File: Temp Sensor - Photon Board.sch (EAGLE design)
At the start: 6 parts

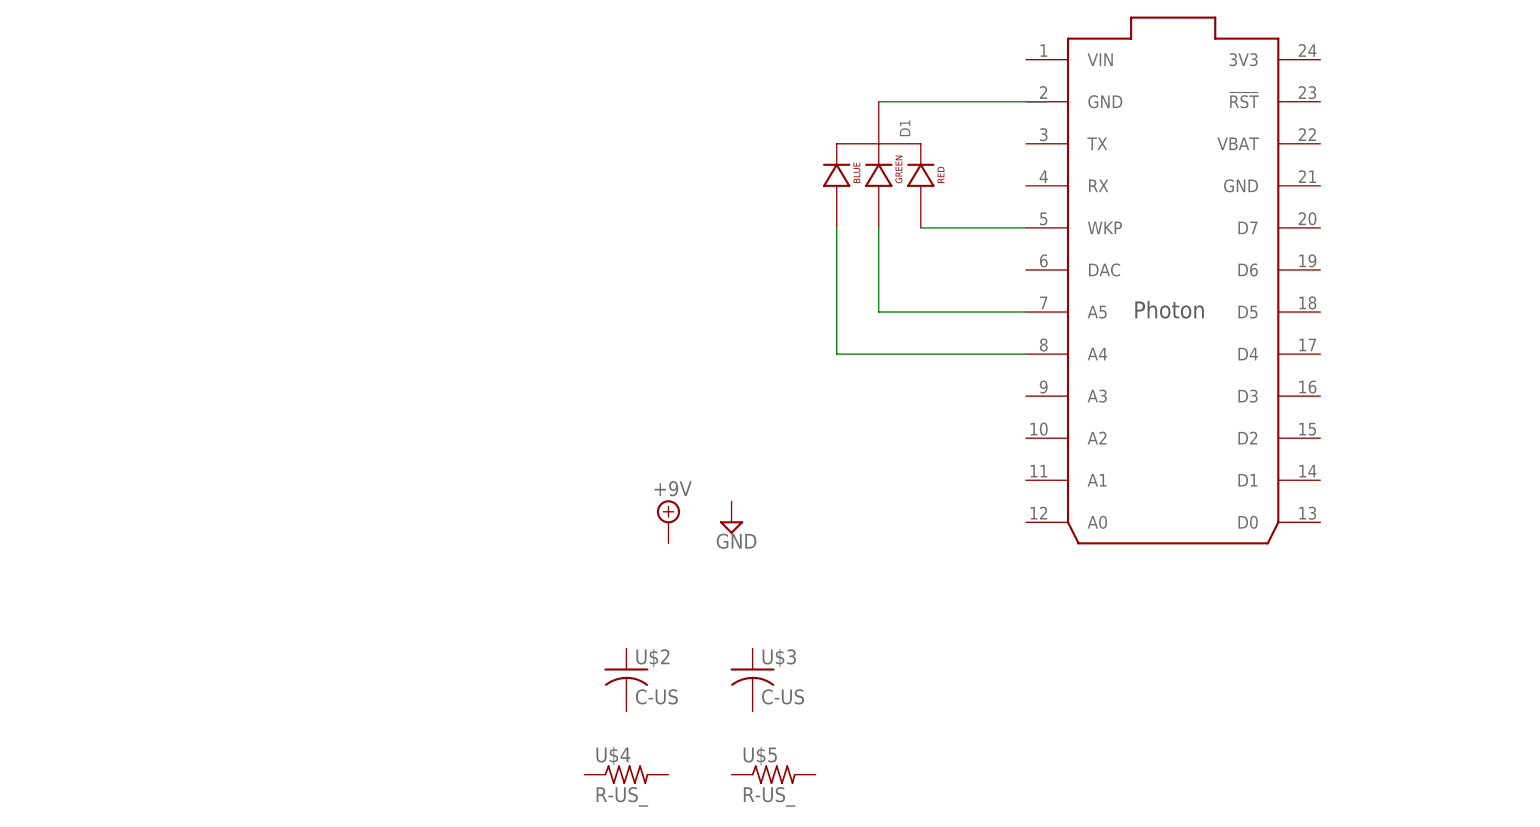
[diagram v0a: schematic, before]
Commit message: Added Photon Board schematics and board
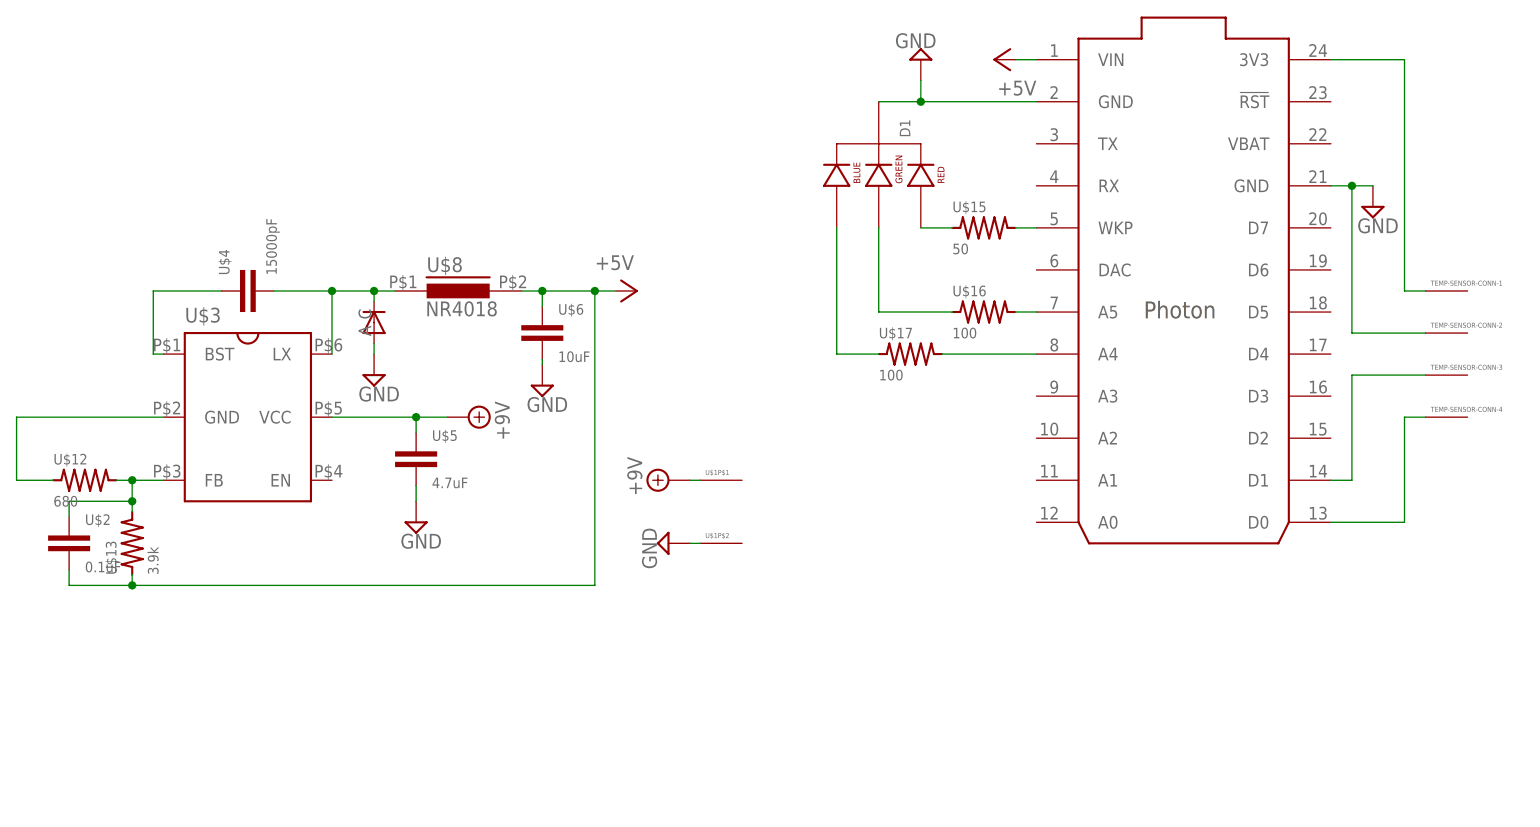
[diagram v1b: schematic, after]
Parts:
- added TEMP-SENSOR-CONN-: (no value), myhvac:S4B-PH-K-S
- added U$11: Photon w/ Headers, Spark:PHOTON_WITH_HEADERS
- added U$12: 680, myhvac:R0805
- added U$13: 3.9k, myhvac:R0805
- added U$15: 50, myhvac:R0805
- added U$16, U$17: 100, myhvac:R0805
- added U$6: 10uF, myhvac:FK16X7R1E106K
- added U$7: RK16, myhvac:RK16
- added U$8: NR4018, myhvac:NR4018
- D1: value LED-RGB-CC-THRUDIFFUSE -> LED-RGB-CC-THRU; device SparkFun-LED:LED-RGB-CC-THRUDIFFUSE -> myhvac:LED-RGB-CC-THRU
- U$1: value PHOTON_SMD -> (none); device Spark:PHOTON_SMD -> myhvac:S2B-PH-K-S
- U$2: value C-US -> 0.1uF; device Spark:C-US -> myhvac:K104Z15Y5VE5TL2
- U$3: value C-US -> (none); device Spark:C-US -> myhvac:BD9G101G-TR
- U$4: value R-US_ -> 15000pF; device Spark:R-US_ -> myhvac:K153K10X7RF5UH5
- U$5: value R-US_ -> 4.7uF; device Spark:R-US_ -> myhvac:FK28C0G1H4R7C
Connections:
- new net +5V: U$11.VIN, U$13.P$1, U$2.P$2, U$6.P$1, U$8.2
- new net +9V: U$1P$1.P$1, U$3.VCC, U$5.P$1
- new net GND: D1.CATHODE, TEMP-SENSOR-CONN-2.P$1, U$11.GND@2, U$11.GND@21, U$1P$2.P$1, U$5.P$2, U$6.P$2, U$7.ANODE
- new net N$11: U$11.A5, U$16.P$2
- new net N$12: U$11.A4, U$17.P$2
- new net N$13: D1.RED_CATHODE, U$15.P$1
- new net N$18: U$12.P$1, U$3.GND
- new net N$5: U$3.LX, U$4.P$2, U$7.CATHODE, U$8.1
- new net N$6: U$12.P$2, U$13.P$2, U$2.P$1, U$3.FB
- new net N$7: TEMP-SENSOR-CONN-1.P$1, U$11.3V3
- new net N$8: TEMP-SENSOR-CONN-3.P$1, U$11.D1
- new net N$9: TEMP-SENSOR-CONN-4.P$1, U$11.D0
- net N$1: now also U$11.WKP, U$15.P$2; no longer D1.RED_CATHODE, U$1G$1.WKP
- net N$2: now also U$16.P$1; no longer U$1G$1.A5
- net N$3: now also U$17.P$1; no longer U$1G$1.A4
- net N$4: now also U$3.BST, U$4.P$1; no longer D1.CATHODE

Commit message: Added Temp Sensor gerber files.  General cleanup or bck files
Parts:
- U$15: value 50 -> 100
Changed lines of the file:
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@@
 <part name="P+1" library="supply1" deviceset="+5V" device=""/>
 <part name="P+2" library="supply1" deviceset="+5V" device=""/>
-<part name="U$15" library="myhvac" deviceset="R0805" device="" value="50"/>
+<part name="U$15" library="myhvac" deviceset="R0805" device="" value="100"/>
 <part name="U$16" library="myhvac" deviceset="R0805" device="" value="100"/>
 <part name="U$17" library="myhvac" deviceset="R0805" device="" value="100"/>
@@
 </sheet>
 </sheets>
+<errors>
+</errors>
 </schematic>
 </drawing>

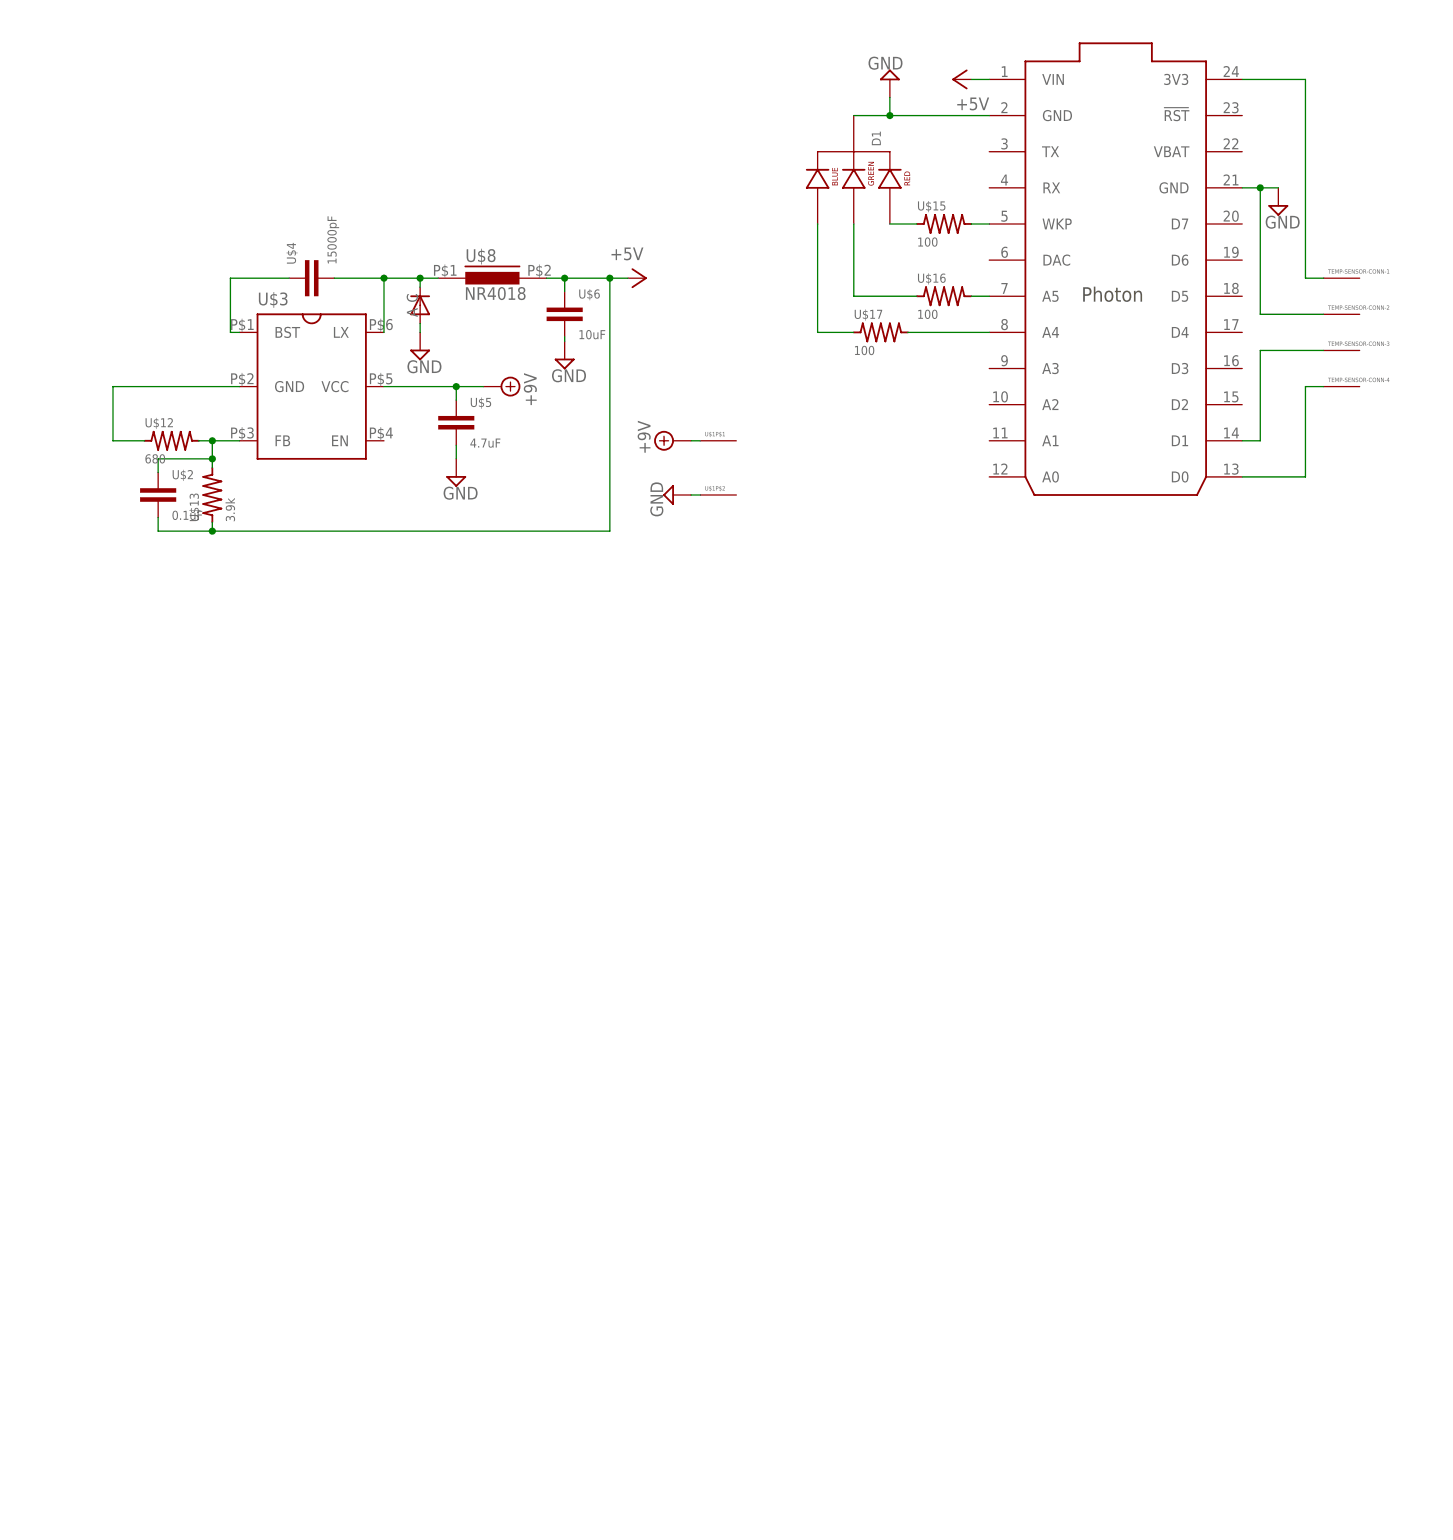
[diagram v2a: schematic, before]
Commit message: Modified the temp sensor to use a prebuilt power converter
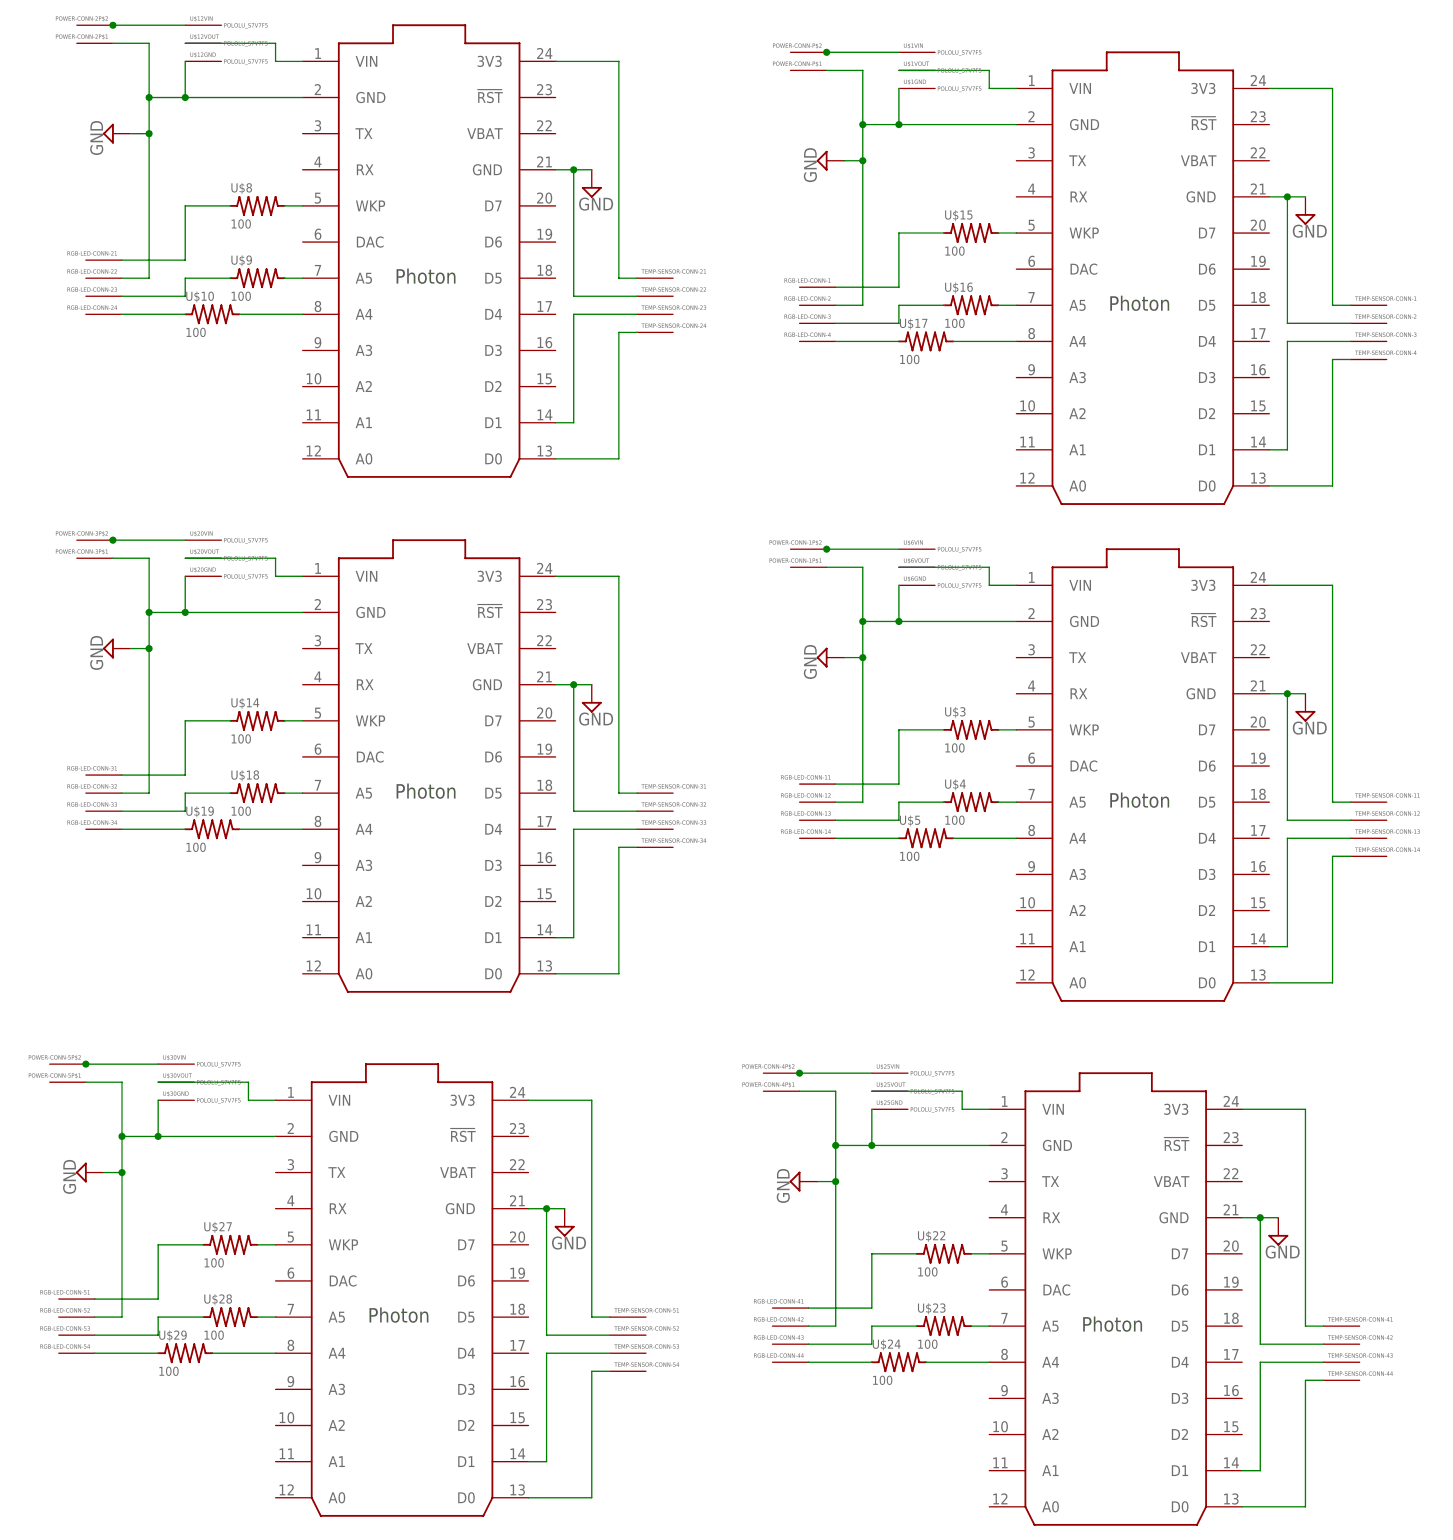
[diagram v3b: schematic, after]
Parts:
- removed D1: LED-RGB-CC-THRU, myhvac:LED-RGB-CC-THRU
- added POWER-CONN-, POWER-CONN-1, POWER-CONN-2, POWER-CONN-3, POWER-CONN-4, POWER-CONN-5: (no value), myhvac:S2B-PH-K-S
- added RGB-LED-CONN-, RGB-LED-CONN-1, RGB-LED-CONN-2, RGB-LED-CONN-3, RGB-LED-CONN-4, RGB-LED-CONN-5, TEMP-SENSOR-CONN-1, TEMP-SENSOR-CONN-2, TEMP-SENSOR-CONN-3, TEMP-SENSOR-CONN-4, TEMP-SENSOR-CONN-5: (no value), myhvac:S4B-PH-K-S
- added U$10, U$14, U$18, U$19, U$22, U$23, U$24, U$27, U$28, U$29, U$9: 100, myhvac:R0805
- added U$20, U$25, U$30: POLOLU_S7V7F5, myhvac:POLOLU_S7V7F5
- added U$21, U$26: Photon w/ Headers, Spark:PHOTON_WITH_HEADERS
- U$1: value (none) -> POLOLU_S7V7F5; device myhvac:S2B-PH-K-S -> myhvac:POLOLU_S7V7F5
- U$12: value 680 -> POLOLU_S7V7F5; device myhvac:R0805 -> myhvac:POLOLU_S7V7F5
- U$13: value 3.9k -> Photon w/ Headers; device myhvac:R0805 -> Spark:PHOTON_WITH_HEADERS
- U$2: value 0.1uF -> Photon w/ Headers; device myhvac:K104Z15Y5VE5TL2 -> Spark:PHOTON_WITH_HEADERS
- U$3: value (none) -> 100; device myhvac:BD9G101G-TR -> myhvac:R0805
- U$4: value 15000pF -> 100; device myhvac:K153K10X7RF5UH5 -> myhvac:R0805
- U$5: value 4.7uF -> 100; device myhvac:FK28C0G1H4R7C -> myhvac:R0805
- U$6: value 10uF -> POLOLU_S7V7F5; device myhvac:FK16X7R1E106K -> myhvac:POLOLU_S7V7F5
- U$7: value RK16 -> Photon w/ Headers; device myhvac:RK16 -> Spark:PHOTON_WITH_HEADERS
- U$8: value NR4018 -> 100; device myhvac:NR4018 -> myhvac:R0805
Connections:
- removed net +5V: U$11.VIN, U$13.P$1, U$2.P$2, U$6.P$1, U$8.2
- removed net +9V: U$1P$1.P$1, U$3.VCC, U$5.P$1
- new net N$10: RGB-LED-CONN-14.P$1, U$5.P$1
- new net N$14: TEMP-SENSOR-CONN-11.P$1, U$2.3V3
- new net N$15: TEMP-SENSOR-CONN-13.P$1, U$2.D1
- new net N$16: TEMP-SENSOR-CONN-14.P$1, U$2.D0
- new net N$17: U$2.WKP, U$3.P$2
- new net N$19: U$2.A4, U$5.P$2
- new net N$20: RGB-LED-CONN-11.P$1, U$3.P$1
- new net N$21: U$2.VIN, U$6VOUT.P$1
- new net N$22: POWER-CONN-1P$2.P$1, U$6VIN.P$1
- new net N$23: RGB-LED-CONN-23.P$1, U$9.P$1
- new net N$24: RGB-LED-CONN-24.P$1, U$10.P$1
- new net N$25: TEMP-SENSOR-CONN-21.P$1, U$7.3V3
- new net N$26: TEMP-SENSOR-CONN-23.P$1, U$7.D1
- new net N$27: TEMP-SENSOR-CONN-24.P$1, U$7.D0
- new net N$28: U$7.WKP, U$8.P$2
- new net N$29: U$7.A5, U$9.P$2
- new net N$30: U$10.P$2, U$7.A4
- new net N$31: RGB-LED-CONN-21.P$1, U$8.P$1
- new net N$32: U$12VOUT.P$1, U$7.VIN
- new net N$33: POWER-CONN-2P$2.P$1, U$12VIN.P$1
- new net N$34: RGB-LED-CONN-33.P$1, U$18.P$1
- new net N$35: RGB-LED-CONN-34.P$1, U$19.P$1
- new net N$36: TEMP-SENSOR-CONN-31.P$1, U$13.3V3
- new net N$37: TEMP-SENSOR-CONN-33.P$1, U$13.D1
- new net N$38: TEMP-SENSOR-CONN-34.P$1, U$13.D0
- new net N$39: U$13.WKP, U$14.P$2
- new net N$40: U$13.A5, U$18.P$2
- new net N$41: U$13.A4, U$19.P$2
- new net N$42: RGB-LED-CONN-31.P$1, U$14.P$1
- new net N$43: U$13.VIN, U$20VOUT.P$1
- new net N$44: POWER-CONN-3P$2.P$1, U$20VIN.P$1
- new net N$45: RGB-LED-CONN-43.P$1, U$23.P$1
- new net N$46: RGB-LED-CONN-44.P$1, U$24.P$1
- new net N$47: TEMP-SENSOR-CONN-41.P$1, U$21.3V3
- new net N$48: TEMP-SENSOR-CONN-43.P$1, U$21.D1
- new net N$49: TEMP-SENSOR-CONN-44.P$1, U$21.D0
- new net N$50: U$21.WKP, U$22.P$2
- new net N$51: U$21.A5, U$23.P$2
- new net N$52: U$21.A4, U$24.P$2
- new net N$53: RGB-LED-CONN-41.P$1, U$22.P$1
- new net N$54: U$21.VIN, U$25VOUT.P$1
- new net N$55: POWER-CONN-4P$2.P$1, U$25VIN.P$1
- new net N$56: RGB-LED-CONN-53.P$1, U$28.P$1
- new net N$57: RGB-LED-CONN-54.P$1, U$29.P$1
- new net N$58: TEMP-SENSOR-CONN-51.P$1, U$26.3V3
- new net N$59: TEMP-SENSOR-CONN-53.P$1, U$26.D1
- new net N$60: TEMP-SENSOR-CONN-54.P$1, U$26.D0
- new net N$61: U$26.WKP, U$27.P$2
- new net N$62: U$26.A5, U$28.P$2
- new net N$63: U$26.A4, U$29.P$2
- new net N$64: RGB-LED-CONN-51.P$1, U$27.P$1
- new net N$65: U$26.VIN, U$30VOUT.P$1
- new net N$66: POWER-CONN-5P$2.P$1, U$30VIN.P$1
- net GND: now also POWER-CONN-1P$1.P$1, POWER-CONN-2P$1.P$1, POWER-CONN-3P$1.P$1, POWER-CONN-4P$1.P$1, POWER-CONN-5P$1.P$1, POWER-CONN-P$1.P$1, RGB-LED-CONN-12.P$1, RGB-LED-CONN-2.P$1, RGB-LED-CONN-22.P$1, RGB-LED-CONN-32.P$1, RGB-LED-CONN-42.P$1, RGB-LED-CONN-52.P$1, TEMP-SENSOR-CONN-12.P$1, TEMP-SENSOR-CONN-22.P$1, TEMP-SENSOR-CONN-32.P$1, TEMP-SENSOR-CONN-42.P$1, TEMP-SENSOR-CONN-52.P$1, U$12GND.P$1, U$13.GND@2, U$13.GND@21, U$1GND.P$1, U$2.GND@2, U$2.GND@21, U$20GND.P$1, U$21.GND@2, U$21.GND@21, U$25GND.P$1, U$26.GND@2, U$26.GND@21, U$30GND.P$1, U$6GND.P$1, U$7.GND@2, U$7.GND@21; no longer D1.CATHODE, U$1P$2.P$1, U$5.P$2, U$6.P$2, U$7.ANODE
- net N$13: now also RGB-LED-CONN-1.P$1; no longer D1.RED_CATHODE
- net N$18: now also U$2.A5, U$4.P$2; no longer U$12.P$1, U$3.GND
- net N$2: now also RGB-LED-CONN-3.P$1; no longer D1.GREEN_CATHODE
- net N$3: now also RGB-LED-CONN-4.P$1; no longer D1.BLUE_CATHODE
- net N$4: now also U$11.VIN, U$1VOUT.P$1; no longer U$3.BST, U$4.P$1
- net N$5: now also POWER-CONN-P$2.P$1, U$1VIN.P$1; no longer U$3.LX, U$4.P$2, U$7.CATHODE, U$8.1
- net N$6: now also RGB-LED-CONN-13.P$1, U$4.P$1; no longer U$12.P$2, U$13.P$2, U$2.P$1, U$3.FB
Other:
- moved on the sheet: TEMP-SENSOR-CONN-1, TEMP-SENSOR-CONN-2, TEMP-SENSOR-CONN-3, TEMP-SENSOR-CONN-4, U$15, U$16, U$17
